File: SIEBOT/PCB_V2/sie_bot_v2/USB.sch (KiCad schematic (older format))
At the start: 35 parts, among them J3 USB_2A, U4 GL850G, U5 RCLAMP0502B, U6 RCLAMP0502B, U7 RCLAMP0502B, U8 RCLAMP0502B, X2 12MHz

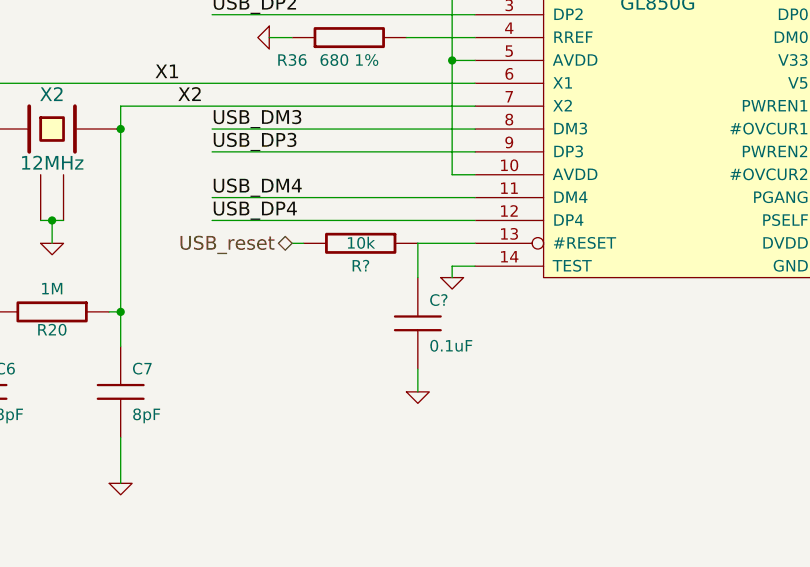
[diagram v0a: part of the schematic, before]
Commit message: Corrección de unos errores entre el PCB y el esquemático
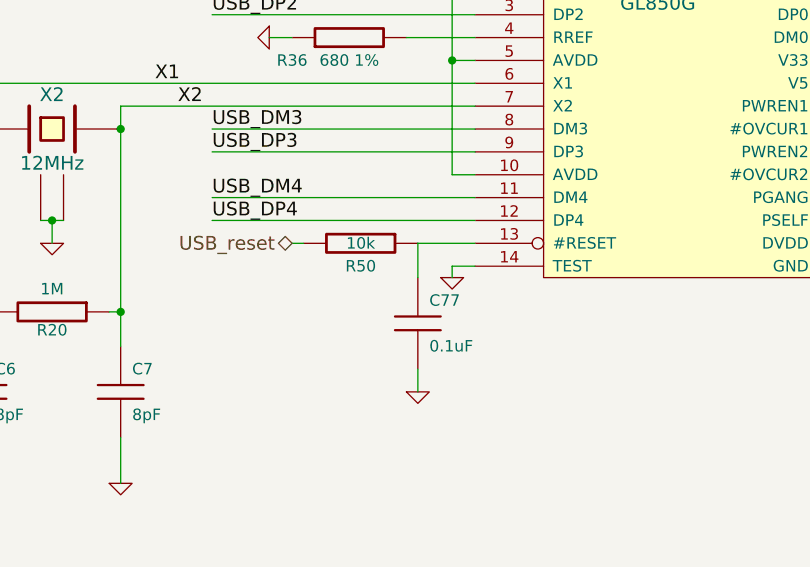
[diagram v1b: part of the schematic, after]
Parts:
- gave numbers to parts that had none: 2
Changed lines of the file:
@@
-EESchema Schematic File Version 2  date sáb 03 mar 2012 09:20:54 COT
+EESchema Schematic File Version 2  date Fri 30 Mar 2012 08:38:46 AM COT
 LIBS:con-jack
 LIBS:adm3101e
@@
 LIBS:zxmhc3f381n8
 LIBS:i.mx233stamp-cache
-EELAYER 24  0
+EELAYER 25  0
 EELAYER END
 $Descr A4 11700 8267
+encoding utf-8
 Sheet 5 5
 Title ""
-Date "3 mar 2012"
+Date "30 mar 2012"
 Rev ""
 Comp ""
@@
 	6550 3200 6800 3200
 $Comp
-L C C?
+L C C77
 U 1 1 4F522649
 P 6550 3550
-F 0 "C?" H 6600 3650 50  0000 L CNN
+F 0 "C77" H 6600 3650 50  0000 L CNN
 F 1 "0.1uF" H 6600 3450 50  0000 L CNN
 F 2 "SM0603" H 6550 3550 60  0001 C CNN
@@
 $EndComp
 $Comp
-L R R?
+L R R50
 U 1 1 4F522458
 P 6300 3200
-F 0 "R?" V 6400 3200 50  0000 C CNN
+F 0 "R50" V 6400 3200 50  0000 C CNN
 F 1 "10k" V 6300 3200 50  0000 C CNN
 F 2 "SM0603" H 6300 3200 60  0001 C CNN

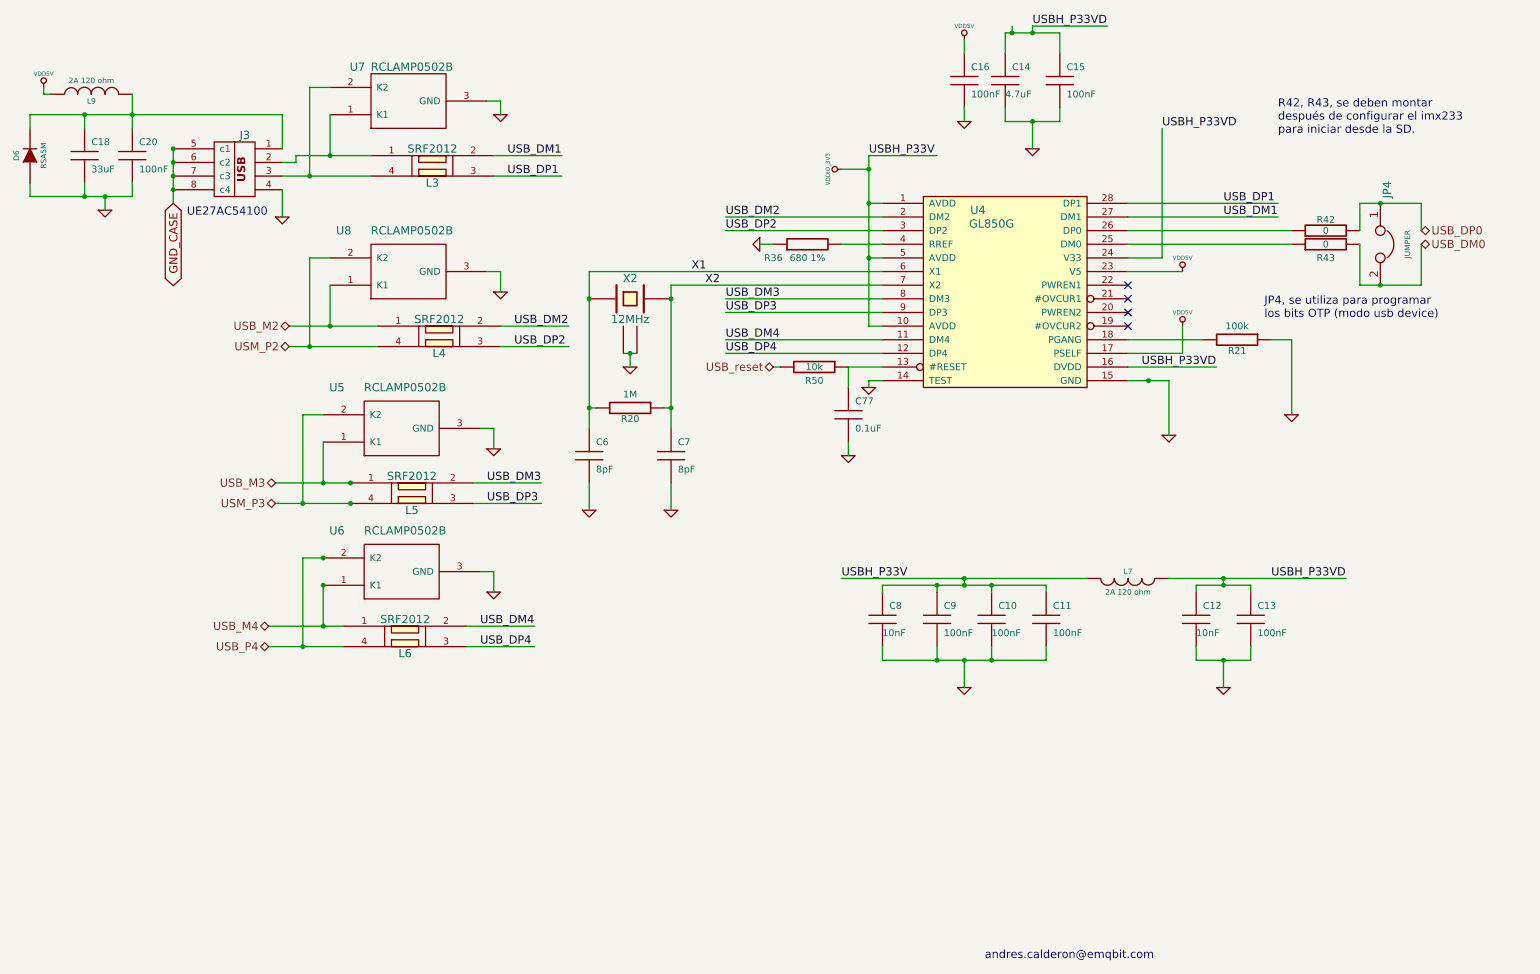
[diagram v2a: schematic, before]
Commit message: USB device connector has been added
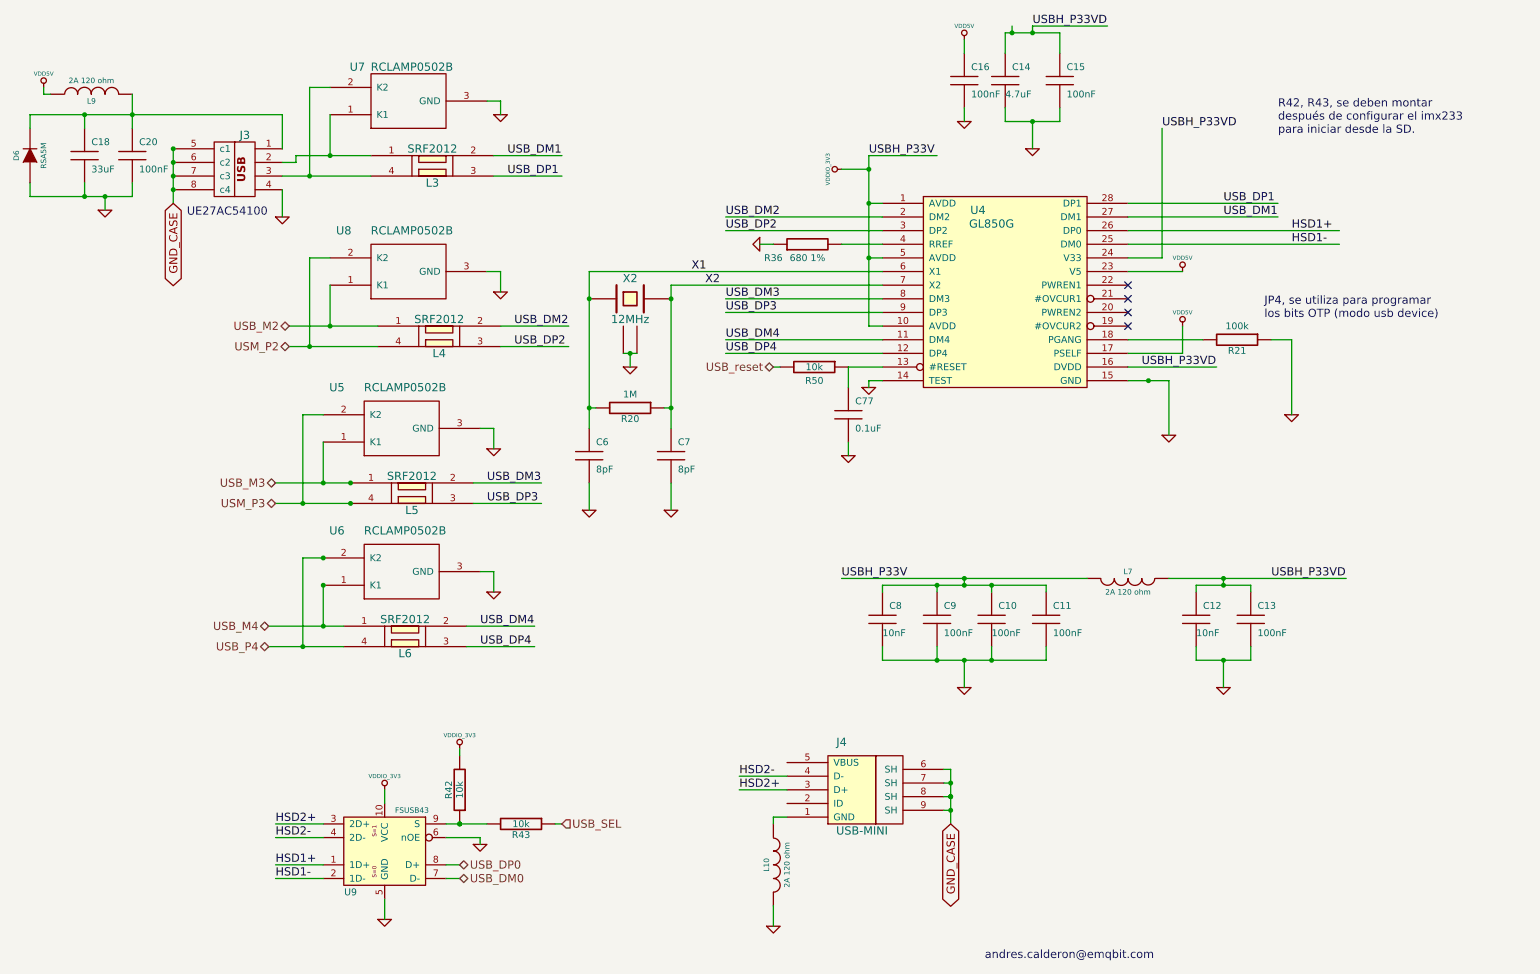
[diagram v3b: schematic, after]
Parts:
- removed JP4: JUMPER, PIN_ARRAY_2X1, symbol JUMPER
- added J4: USB-MINI, miniUSB_B, symbol USB-MINI
- added L10: 2A 120 ohm, SM0805, symbol INDUCTOR
- added U9: FSUSB43, lead10_micropak, symbol FSUSB43
- R42, R43: value 0 -> 10k
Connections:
- net labels added: HSD1+, HSD1-, HSD2+, HSD2-, USB_SEL
- wire segments 137 -> 154
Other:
- moved on the sheet: R42
